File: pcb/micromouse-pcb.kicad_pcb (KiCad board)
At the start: 2 copper layers, 150 x 185 mm, 108 parts, among them J1 JST_XH_B2B-XH-A_1x02_P2.50mm_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, J10 PinSocket_1x08_P2.54mm_Vertic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, J11 PinSocket_1x08_P2.54mm_Vertic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, J12 PinSocket_1x15_P2.54mm_Vertic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, J13 PinSocket_1x15_P2.54mm_Vertic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, J2 PinHeader_1x02_P2.54mm_Vertic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, J3 JST_XH_B3B-XH-A_1x03_P2.50mm_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, J4 PinSocket_1x15_P2.54mm_Vertic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, J5 JST_PH_B6B-PH-K_1x06_P2.00mm_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, J6 JST_PH_B6B-PH-K_1x06_P2.00mm_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, J8 PinSocket_1x15_P2.54mm_Vertic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, Q1 SOT-23, Q10 LED_D3.0mm_Clear, Q11 SOT-23, Q12 LED_D3.0mm_Clear, Q13 SOT-23, Q14 LED_1206_3216Metric, Q15 SOT-23, Q16 LED_1206_3216Metric, Q17 SOT-23, Q18 LED_1206_3216Metric, Q19 SOT-23, Q2 LED_D3.0mm_Clear, Q20 LED_1206_3216Metric, Q21 SOT-23, Q22 LED_1206_3216Metric, Q23 SOT-23, Q24 LED_1206_3216Metric, Q25 SOT-23, Q26 LED_1206_3216Metric, Q27 SOT-23, Q28 LED_1206_3216Metric, Q29 SOT-23, Q3 SOT-23, Q4 LED_D3.0mm_Clear, Q5 SOT-23, Q6 LED_D3.0mm_Clear, Q7 SOT-23, Q8 LED_D3.0mm_Clear, Q9 SOT-23, SW1 SW_PUSH_6mm, U1 TSOT-23-6, U4 SOIC-24W_7.5x15.4mm_P1.27mm, U5 SOIC-24W_7.5x15.4mm_P1.27mm

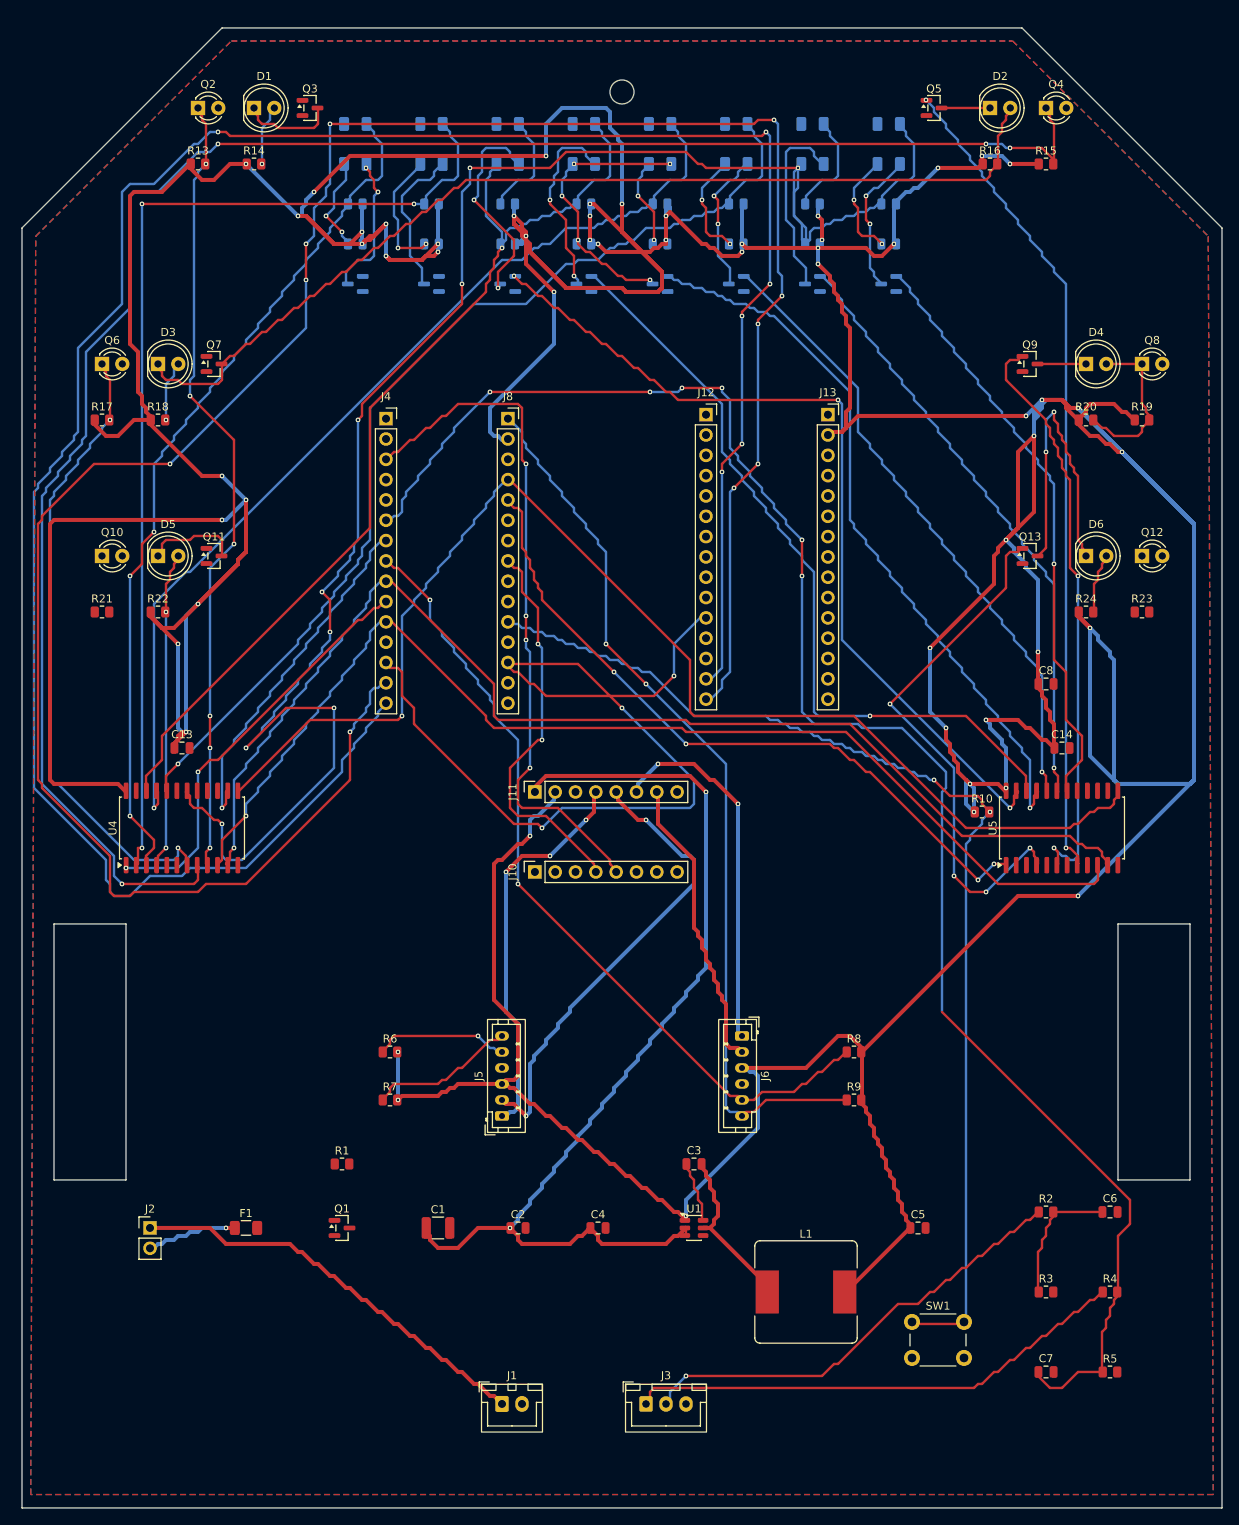
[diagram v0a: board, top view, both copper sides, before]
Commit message: Rev 2: ESP32-only redesign -- 100x128mm, 4 layers, DRC-clean
Drop the STM32 entirely (user decision): one socketed Arduino Nano ESP32
(real Module:Arduino_Nano footprint, pad map locked to the USB marker)
now does all control + telemetry. All control nets kept their names and
moved to A1; ADC nets on A0-A2; UART flash relay removed.

Board shrinks 150x185 -> 100x128mm (chamfered, wheels inside via interior
slots). In-house router generalized to N layers (THT pierces all, SMD its
face, through-vias join, per-layer H/V discipline) + a 0.25mm fine-grid
retry pass: 2012 tracks / 150 vias on 4 signal layers, 5 edges left for
the GUI. ERC 0, DRC 0 errors.

Also: wall-sensor side clusters with rotated THT LEDs (fixes a real
THT-into-bottom-SMD short), castor hole moved out of the line array,
smaller buck inductor (SRP7028A), CONNECTIONS.md fully regenerated for
the ESP32-only design (96 nets, coverage-enforced).

Co-Authored-By: Claude Fable 5 <noreply@anthropic.com>
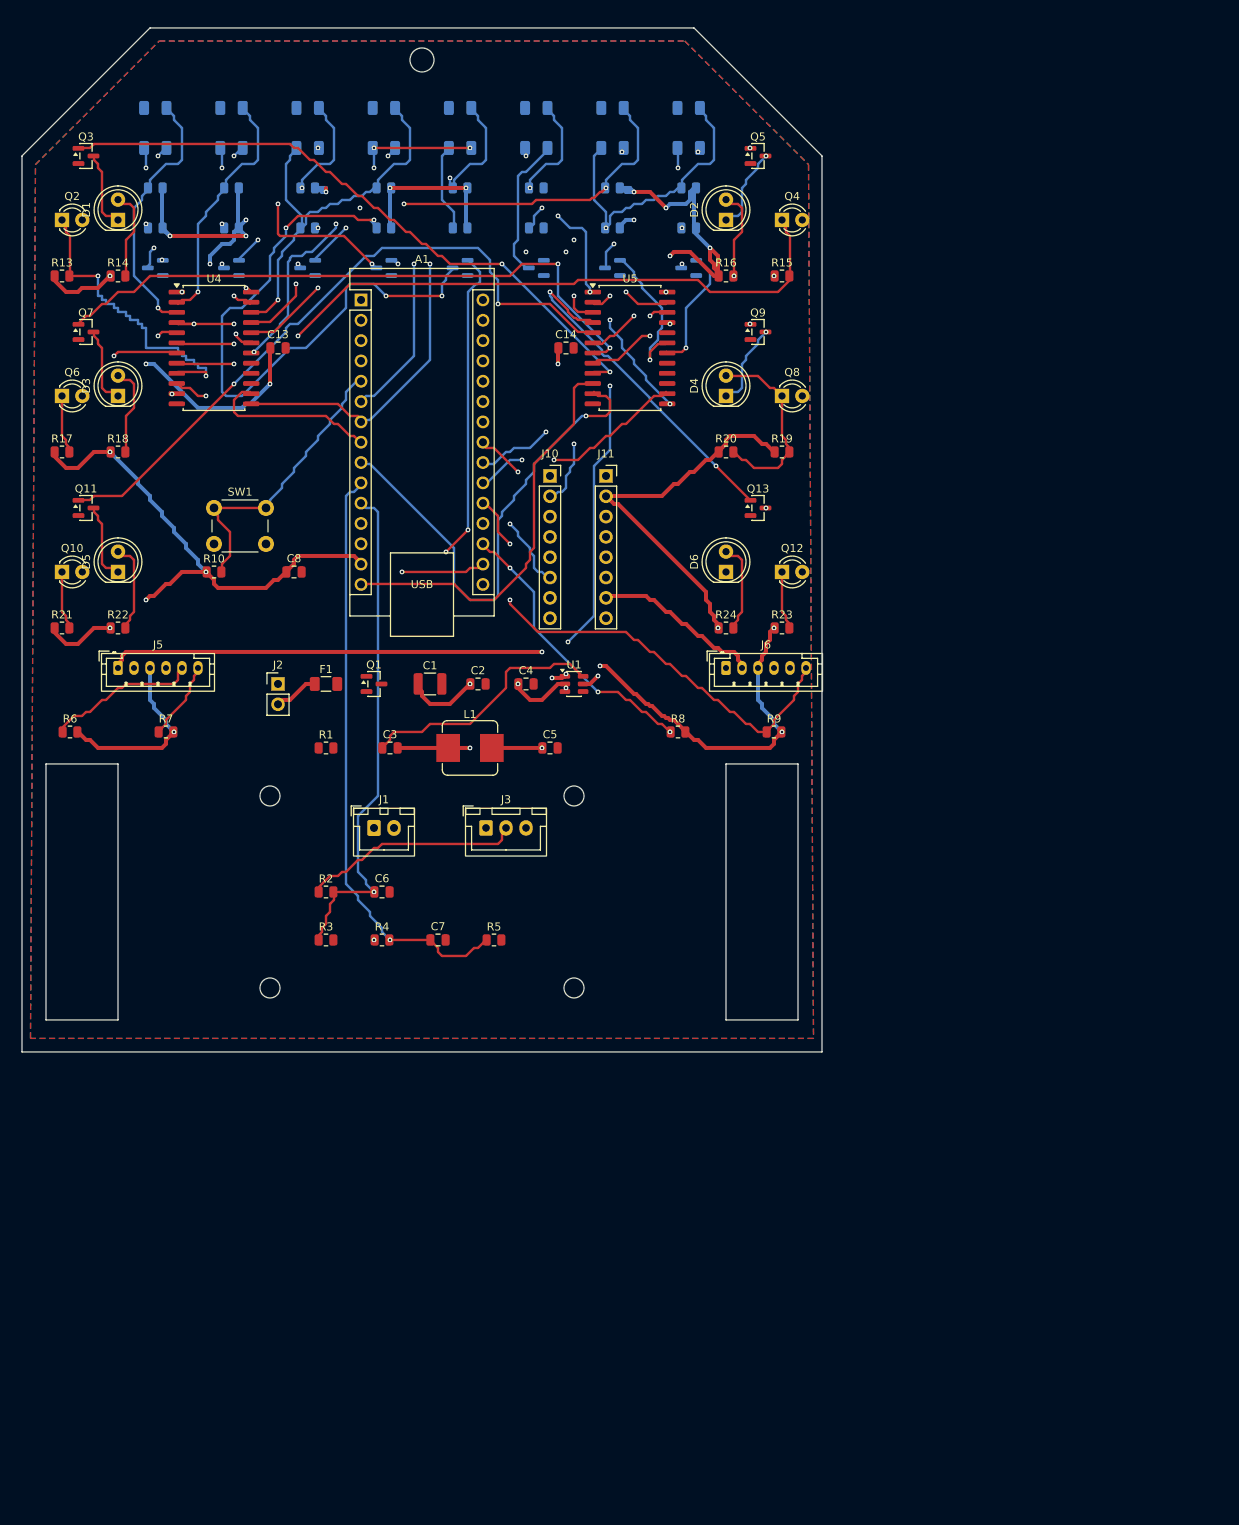
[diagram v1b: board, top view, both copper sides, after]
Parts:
- removed J12, J13, J4, J8: PinSocket_1x15_P2.54mm_Vertical, PinSocket_1x15_P2.54mm_Vertical
- added A1: Arduino_Nano, Arduino_Nano, F.Cu at (42.4, 34.0)
- L1: value L_Bourns_SRR1260 -> 3.3uH; footprint L_Bourns_SRR1260 -> L_Bourns_SRP7028A_7.3x6.6mm
- moved SW1 134.0 mm to (24.0, 60.0)
- moved R4 101.1 mm to (45.0, 114.0)
- moved R10 100.6 mm to (24.0, 68.0)
- moved R3 100.2 mm to (38.0, 114.0)
- moved C6 99.4 mm to (45.0, 108.0)
- moved R2 98.5 mm to (38.0, 108.0)
- moved C8 95.0 mm to (34.0, 68.0)
- moved R5 94.0 mm to (59.0, 114.0)
- moved C7 93.2 mm to (52.0, 114.0)
- moved U5 80.7 mm to (76.0, 40.0), turned to 0 degrees
- moved L1 79.9 mm to (56.0, 90.0)
- moved C14 79.6 mm to (68.0, 40.0)
- moved C5 75.6 mm to (66.0, 90.0)
- moved J3 74.7 mm to (58.0, 100.0)
- moved J1 73.8 mm to (44.0, 100.0)
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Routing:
- net PLUS3V3: track 1258.3 -> 482.8 mm, vias 55 -> 32
- net USART1_RX: track 304.2 -> 0.00 mm, vias 10 -> 0
- net USART1_TX: track 299.0 -> 0.00 mm, vias 6 -> 0
- net WALL2_SENSE: track 233.7 -> 90.4 mm, vias 4 -> 2
- net VBAT_PACK_SENSE: track 213.7 -> 74.9 mm, vias 6 -> 1
- net LINE8_SENSE: track 225.6 -> 94.3 mm, vias 9 -> 3
- net NRST: track 117.8 -> 0.00 mm, vias 3 -> 0
- net WALL6_SENSE: track 40.0 -> 151.9 mm
- net USER_BTN: track 144.6 -> 37.3 mm, vias 2 -> 0
- net LINE2_SENSE: track 132.2 -> 31.7 mm, vias 3 -> 1
- net WALL5_LED: track 0.00 -> 85.1 mm, vias 0 -> 2
- net MUX_S3: track 160.9 -> 78.8 mm, vias 1 -> 3
- net LINE6_LED: track 80.9 -> 0.00 mm, vias 1 -> 0
- net WALL1_LED: track 0.00 -> 80.8 mm, vias 0 -> 2
- net WALL4_SENSE: track 21.1 -> 101.3 mm, vias 0 -> 1
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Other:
- board size 150 x 185 mm -> 100 x 128 mm
- copper layers 2 -> 4

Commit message: Rev 3: line indicator LEDs, research-verified sensor geometry, 100x114mm
User requests: per-channel indicator LEDs on top, professional wall-sensor
positioning, smaller/tighter board.

- 8 indicator LEDs (D15-D22 + 1k + BSS138, gate on each LINEx_SENSE):
  zero DC load on the analog nodes; crisp threshold indication (LED ON =
  dark line). Adversarial review caught duty-cycle blindness (pulsed
  emitters leave nodes ambient-dominated ~93% of the time) -- fixed by
  dropping line emitters 33R -> 120R (~15mA) so firmware can latch all 8
  on continuously in line-follow mode. BOM: super-red AlInGaP indicators
  + daylight-filtered line receivers REQUIRED (optical feedback).

- Wall sensors repositioned per primary-source research (Harrison Decimus,
  UKMARS, Zeetah): front pair (toe-out) 89mm ahead of the axle, 45-deg
  diagonals ON the chamfered corners 74mm, side pair (forward toe) 56mm --
  all well in front of the center of rotation, per the verbatim Decimus
  6-sensor doctrine. Assembly aiming/shielding notes in PROJECT_NOTES.

- Board 100x128 -> 100x114: controller rotated horizontal, muxes to the
  side edges, axle forward to y=92, mounting holes added as router
  obstacles. 2139 tracks / 179 vias on 4 layers, ERC 0, DRC 0 errors,
  9 edges left for GUI finishing.

Co-Authored-By: Claude Fable 5 <noreply@anthropic.com>
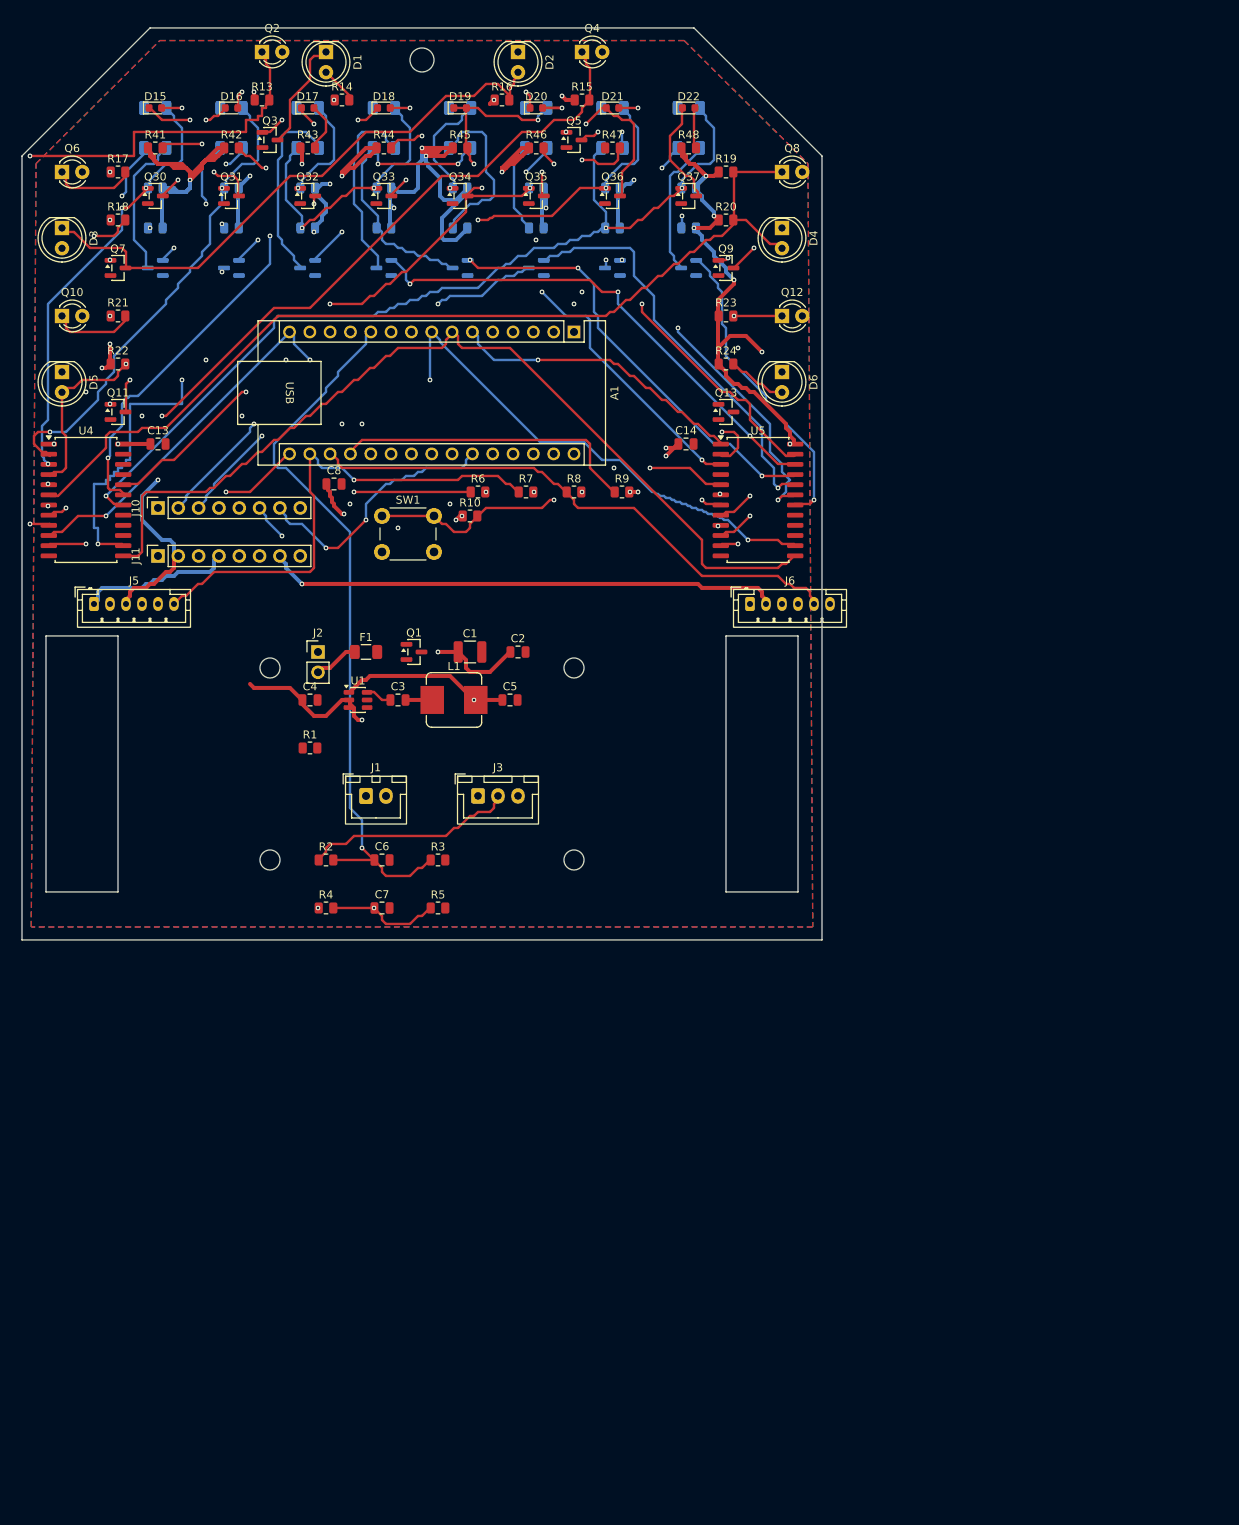
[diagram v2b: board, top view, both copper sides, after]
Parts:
- added D15: Indicator LED 0603 super-red AlInGaP, high-efficiency bin R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, LED_0603_1608Metric, F.Cu at (16.7, 10.0)
- added D16: Indicator LED 0603 super-red AlInGaP, high-efficiency bin R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, LED_0603_1608Metric, F.Cu at (26.2, 10.0)
- added D17: Indicator LED 0603 super-red AlInGaP, high-efficiency bin R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, LED_0603_1608Metric, F.Cu at (35.7, 10.0)
- added D18: Indicator LED 0603 super-red AlInGaP, high-efficiency bin R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, LED_0603_1608Metric, F.Cu at (45.2, 10.0)
- added D19: Indicator LED 0603 super-red AlInGaP, high-efficiency bin R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, LED_0603_1608Metric, F.Cu at (54.8, 10.0)
- added D20: Indicator LED 0603 super-red AlInGaP, high-efficiency bin R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, LED_0603_1608Metric, F.Cu at (64.3, 10.0)
- added D21: Indicator LED 0603 super-red AlInGaP, high-efficiency bin R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, LED_0603_1608Metric, F.Cu at (73.8, 10.0)
- added D22: Indicator LED 0603 super-red AlInGaP, high-efficiency bin R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, LED_0603_1608Metric, F.Cu at (83.3, 10.0)
- added Q30: SOT-23, SOT-23, F.Cu at (16.7, 21.0)
- added Q31: SOT-23, SOT-23, F.Cu at (26.2, 21.0)
- added Q32: SOT-23, SOT-23, F.Cu at (35.7, 21.0)
- added Q33: SOT-23, SOT-23, F.Cu at (45.2, 21.0)
- added Q34: SOT-23, SOT-23, F.Cu at (54.8, 21.0)
- added Q35: SOT-23, SOT-23, F.Cu at (64.3, 21.0)
- added Q36: SOT-23, SOT-23, F.Cu at (73.8, 21.0)
- added Q37: SOT-23, SOT-23, F.Cu at (83.3, 21.0)
- added R41: R_0805_2012Metric, R_0805_2012Metric, F.Cu at (16.7, 15.0)
- added R42: R_0805_2012Metric, R_0805_2012Metric, F.Cu at (26.2, 15.0)
- added R43: R_0805_2012Metric, R_0805_2012Metric, F.Cu at (35.7, 15.0)
- added R44: R_0805_2012Metric, R_0805_2012Metric, F.Cu at (45.2, 15.0)
- added R45: R_0805_2012Metric, R_0805_2012Metric, F.Cu at (54.8, 15.0)
- added R46: R_0805_2012Metric, R_0805_2012Metric, F.Cu at (64.3, 15.0)
- added R47: R_0805_2012Metric, R_0805_2012Metric, F.Cu at (73.8, 15.0)
- added R48: R_0805_2012Metric, R_0805_2012Metric, F.Cu at (83.3, 15.0)
- Q14, Q16, Q18, Q20, Q22, Q24, Q26, Q28: value LED_1206_3216Metric -> SMD phototransistor 940nm, DAYLIGHT-FILTERED REQUIRED (e.g. Osram SFH320FA -- an unfiltered part re-opens optical feedb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
- R26, R28, R30, R32, R34, R36, R38, R40: value R_0805_2012Metric -> 120
- moved R6 59.2 mm to (57.0, 58.0)
- moved J11 56.9 mm to (17.0, 66.0), turned to 90 degrees
- moved R7 54.1 mm to (63.0, 58.0)
- moved J10 49.2 mm to (17.0, 60.0), turned to 90 degrees
- moved R21 39.6 mm to (12.0, 36.0)
- moved R23 39.6 mm to (88.0, 36.0)
- moved R17 35.7 mm to (12.0, 18.0)
- moved R19 35.7 mm to (88.0, 18.0)
- moved R14 35.6 mm to (40.0, 9.00)
- moved R16 35.6 mm to (60.0, 9.00)
- moved R9 35.5 mm to (75.0, 58.0)
- moved D1 33.4 mm to (38.0, 3.00), turned to -90 degrees
- moved D2 33.4 mm to (62.0, 3.00), turned to -90 degrees
- moved R13 33.3 mm to (30.0, 9.00)
- moved R15 33.3 mm to (70.0, 9.00)
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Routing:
- net PLUS3V3: track 482.8 -> 628.9 mm, vias 32 -> 42
- net Net-(D10-A): track 101.4 -> 39.1 mm, vias 7 -> 2
- net MOTA_P: track 72.9 -> 19.3 mm, vias 1 -> 0
- net LINE5_LED: track 109.2 -> 55.5 mm, vias 5 -> 3
- net LINE6_LED: track 0.00 -> 51.9 mm, vias 0 -> 1
- net MUX_S1: track 89.8 -> 141.5 mm, vias 2 -> 4
- net WALL1_SENSE: track 41.3 -> 92.3 mm
- net MOTA_N: track 70.1 -> 19.8 mm
- net WALL6_SENSE: track 151.9 -> 106.9 mm
- net MOTB_P: track 20.0 -> 64.5 mm
- net WALL6_LED: track 43.8 -> 0.00 mm, vias 2 -> 0
- net MOTB_N: track 21.6 -> 64.6 mm, vias 0 -> 1
- net LINE6_SENSE: track 56.4 -> 98.4 mm, vias 2 -> 6
- net MUX_S2: track 90.6 -> 129.3 mm, vias 1 -> 4
- net MUX_S3: track 78.8 -> 116.0 mm, vias 3 -> 0
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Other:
- board size 100 x 128 mm -> 100 x 114 mm
